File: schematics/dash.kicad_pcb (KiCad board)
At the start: 2 copper layers, 50 x 30 mm, 29 parts, among them J1 BATT_CONN, J2 EXTERNAL_TRIGGER, J3 USB_OTG, SW1 SW_Push, U1 ESP-12E, U2 ch340g, U3 MCP73833, U4 HT7333, Y1 12Mhz

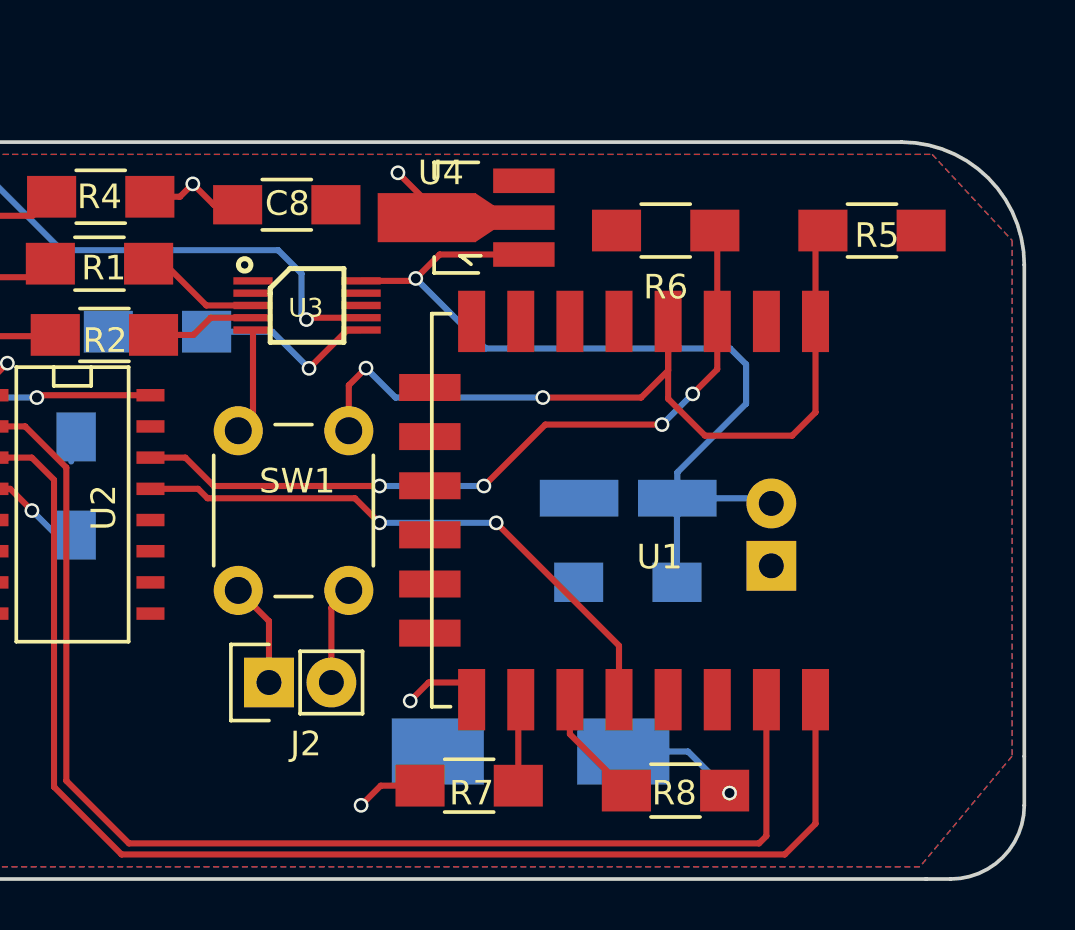
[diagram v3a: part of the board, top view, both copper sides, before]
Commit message: [fix] Correct wiring
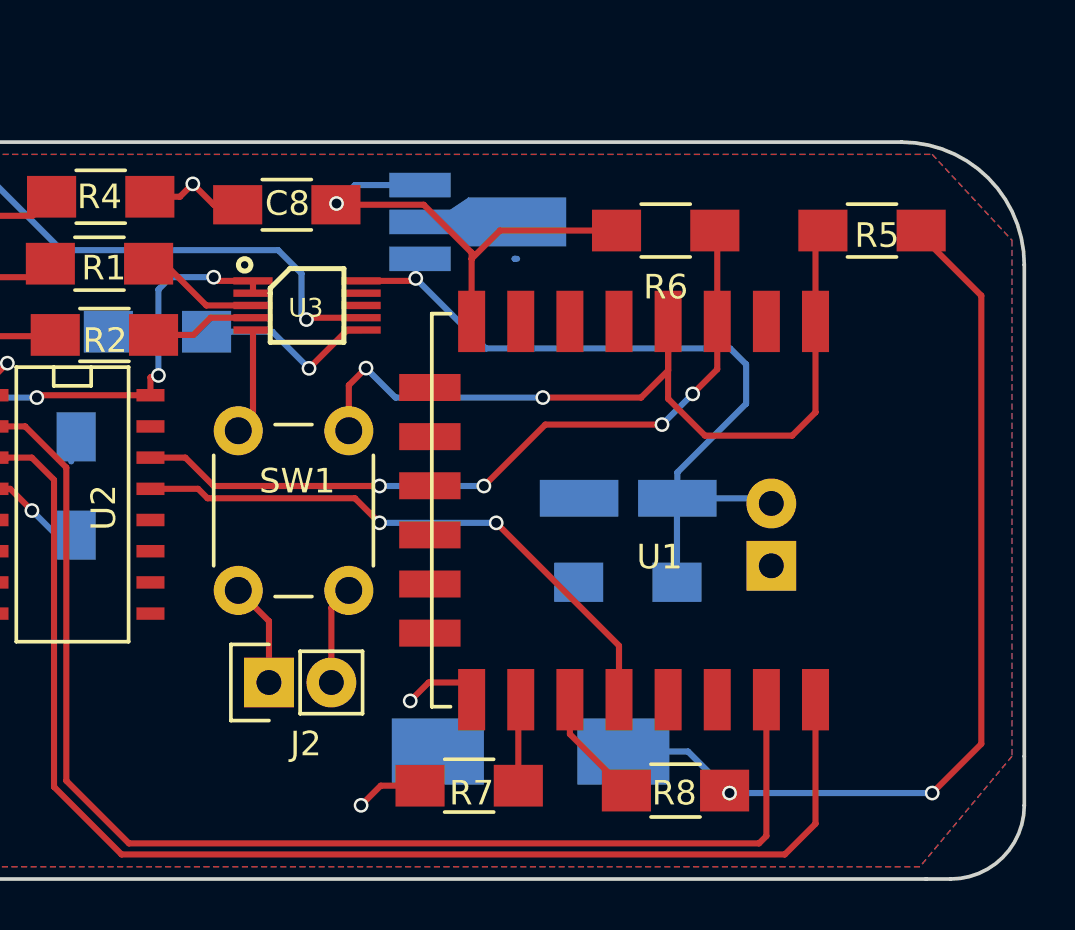
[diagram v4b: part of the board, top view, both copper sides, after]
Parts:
- U4: moved to B.Cu
- moved U4 0.51 mm to (152.8, 98.2)
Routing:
- net +3V3: track 5.27 -> 59.8 mm, vias 1 -> 3
- net +5V: track 26.9 -> 36.1 mm, vias 2 -> 4
- net Net-(C1-Pad1): track 35.9 -> 32.0 mm
- net GND: track 24.6 -> 22.3 mm, vias 6 -> 5
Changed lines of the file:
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@@
   (general
     (links 68)
-    (no_connects 12)
+    (no_connects 5)
     (area 124.924999 94.924999 175.075001 125.075001)
     (thickness 1.6)
     (drawings 10)
-    (tracks 196)
+    (tracks 223)
     (zones 0)
     (modules 29)
@@
     (add_net "Net-(U3-Pad9)")
   )
-  (module TO_SOT_Packages_SMD:SOT89-3_Housing_Handsoldering (layer F.Cu)
-    (at 152.275 98.075 90)
+  (module TO_SOT_Packages_SMD:SOT89-3_Housing_Handsoldering (layer B.Cu)
+    (at 152.75 98.25 90)
     (descr "SOT89-3, Housing, Handsoldering,")
     (tags "SOT89-3, Housing, Handsoldering,")
     (attr smd)
-    (fp_text reference U4 (at 1.825 -1.025 360) (layer F.SilkS)
-      (effects (font (size 1 1) (thickness 0.15)))
-    )
-    (fp_text value HT7333 (at -0.14986 5.30098 90) (layer F.Fab)
-      (effects (font (size 1 1) (thickness 0.15)))
-    )
-    (fp_line (start -1.89992 0.20066) (end -1.651 -0.09906) (layer F.SilkS) (width 0.15))
-    (fp_line (start -1.651 -0.09906) (end -1.5494 -0.24892) (layer F.SilkS) (width 0.15))
-    (fp_line (start -1.5494 -0.24892) (end -1.5494 0.59944) (layer F.SilkS) (width 0.15))
-    (fp_line (start -2.25044 -1.30048) (end -2.25044 0.50038) (layer F.SilkS) (width 0.15))
-    (fp_line (start -2.25044 -1.30048) (end -1.6002 -1.30048) (layer F.SilkS) (width 0.15))
-    (fp_line (start 2.25044 -1.30048) (end 2.25044 0.50038) (layer F.SilkS) (width 0.15))
-    (fp_line (start 2.25044 -1.30048) (end 1.6002 -1.30048) (layer F.SilkS) (width 0.15))
-    (pad 1 smd rect (at -1.50114 2.35204 90) (size 1.00076 2.5019) (layers F.Cu F.Paste F.Mask)
+    (fp_text reference U4 (at 1.825 1.025 180) (layer B.SilkS)
+      (effects (font (size 1 1) (thickness 0.15)) (justify mirror))
+    )
+    (fp_text value HT7333 (at -0.14986 -5.30098 90) (layer B.Fab)
+      (effects (font (size 1 1) (thickness 0.15)) (justify mirror))
+    )
+    (fp_line (start -1.89992 -0.20066) (end -1.651 0.09906) (layer B.SilkS) (width 0.15))
+    (fp_line (start -1.651 0.09906) (end -1.5494 0.24892) (layer B.SilkS) (width 0.15))
+    (fp_line (start -1.5494 0.24892) (end -1.5494 -0.59944) (layer B.SilkS) (width 0.15))
+    (fp_line (start -2.25044 1.30048) (end -2.25044 -0.50038) (layer B.SilkS) (width 0.15))
+    (fp_line (start -2.25044 1.30048) (end -1.6002 1.30048) (layer B.SilkS) (width 0.15))
+    (fp_line (start 2.25044 1.30048) (end 2.25044 -0.50038) (layer B.SilkS) (width 0.15))
+    (fp_line (start 2.25044 1.30048) (end 1.6002 1.30048) (layer B.SilkS) (width 0.15))
+    (pad 1 smd rect (at -1.50114 -2.35204 90) (size 1.00076 2.5019) (layers B.Cu B.Paste B.Mask)
       (net 1 "Net-(C1-Pad1)"))
-    (pad 2 smd rect (at 0 2.35204 90) (size 1.00076 2.5019) (layers F.Cu F.Paste F.Mask)
-      (net 2 GND))
-    (pad 3 smd rect (at 1.50114 2.35204 90) (size 1.00076 2.5019) (layers F.Cu F.Paste F.Mask)
+    (pad 2 smd rect (at 0 -2.35204 90) (size 1.00076 2.5019) (layers B.Cu B.Paste B.Mask)
+      (net 2 GND))
+    (pad 3 smd rect (at 1.50114 -2.35204 90) (size 1.00076 2.5019) (layers B.Cu B.Paste B.Mask)
       (net 36 +3V3))
-    (pad 2 smd rect (at 0 -1.6002 90) (size 1.99898 4.0005) (layers F.Cu F.Paste F.Mask)
-      (net 2 GND))
-    (pad 2 smd trapezoid (at 0 0.7493 270) (size 1.50114 0.7493) (rect_delta 0 0.50038 ) (layers F.Cu F.Paste F.Mask)
+    (pad 2 smd rect (at 0 1.6002 90) (size 1.99898 4.0005) (layers B.Cu B.Paste B.Mask)
+      (net 2 GND))
+    (pad 2 smd trapezoid (at 0 -0.7493 270) (size 1.50114 0.7493) (rect_delta 0 -0.50038 ) (layers B.Cu B.Paste B.Mask)
       (net 2 GND))
     (model TO_SOT_Packages_SMD.3dshapes/SOT89-3_Housing_Handsoldering.wrl
@@
   (segment (start 95.71 54.35) (end 91.71 50.35) (width 0.25) (layer F.Cu) (net 0))
   (segment (start 129.6 120.8) (end 130 120.8) (width 0.25) (layer F.Cu) (net 0))
+  (segment (start 150.225 100.55) (end 150.225 99.9241) (width 0.25) (layer B.Cu) (net 1) (status 800000))
+  (segment (start 150.225 99.9241) (end 150.39796 99.75114) (width 0.25) (layer B.Cu) (net 1) (status C00000))
   (segment (start 160.86 112.92) (end 160.86 109.515) (width 0.25) (layer B.Cu) (net 1))
   (segment (start 160.86 109.515) (end 160.875 109.5) (width 0.25) (layer B.Cu) (net 1))
-  (segment (start 154.62704 99.57614) (end 151.19886 99.57614) (width 0.25) (layer F.Cu) (net 1))
-  (segment (start 151.19886 99.57614) (end 150.225 100.55) (width 0.25) (layer F.Cu) (net 1))
   (segment (start 160.875 109.5) (end 160.875 108.45) (width 0.25) (layer B.Cu) (net 1))
   (segment (start 150.125 100.65) (end 148 100.65) (width 0.25) (layer F.Cu) (net 1))
@@
   (segment (start 142.975 97.55) (end 142 97.55) (width 0.25) (layer F.Cu) (net 2))
   (segment (start 142 97.55) (end 141.15 96.7) (width 0.25) (layer F.Cu) (net 2))
-  (segment (start 150.6748 98.075) (end 150.6748 97.4248) (width 0.25) (layer F.Cu) (net 2))
-  (segment (start 150.6748 97.4248) (end 149.5 96.25) (width 0.25) (layer F.Cu) (net 2))
-  (via (at 149.5 96.25) (size 0.6) (drill 0.4) (layers F.Cu B.Cu) (net 2))
   (segment (start 139.4 97.225) (end 140.625 97.225) (width 0.25) (layer F.Cu) (net 2))
   (via (at 141.15 96.7) (size 0.6) (drill 0.4) (layers F.Cu B.Cu) (net 2))
@@
   (segment (start 166.5 122.75) (end 165.25 124) (width 0.25) (layer F.Cu) (net 28))
   (segment (start 133.075 107.845) (end 133.595 107.845) (width 0.25) (layer F.Cu) (net 28))
+  (segment (start 143.6 100.65) (end 143.6 101.15) (width 0.25) (layer F.Cu) (net 35) (status C00000))
+  (segment (start 139.425 105.305) (end 139.425 104.575) (width 0.25) (layer F.Cu) (net 35) (status 400000))
+  (segment (start 142.15 100.65) (end 143.6 100.65) (width 0.25) (layer F.Cu) (net 35) (status 800000))
+  (segment (start 142 100.5) (end 142.15 100.65) (width 0.25) (layer F.Cu) (net 35))
+  (via (at 142 100.5) (size 0.6) (drill 0.4) (layers F.Cu B.Cu) (net 35))
+  (segment (start 140.25 100.5) (end 142 100.5) (width 0.25) (layer B.Cu) (net 35))
+  (segment (start 139.75 101) (end 140.25 100.5) (width 0.25) (layer B.Cu) (net 35))
+  (segment (start 139.75 104.5) (end 139.75 101) (width 0.25) (layer B.Cu) (net 35))
+  (via (at 139.75 104.5) (size 0.6) (drill 0.4) (layers F.Cu B.Cu) (net 35))
+  (segment (start 139.425 104.575) (end 139.75 104.5) (width 0.25) (layer F.Cu) (net 35))
   (segment (start 128.18014 102.9) (end 128.18014 100.5) (width 0.25) (layer F.Cu) (net 35))
   (segment (start 130.8 108.2) (end 130.8 105.51986) (width 0.25) (layer F.Cu) (net 35))
@@
   (via (at 130.8 108.2) (size 0.6) (drill 0.4) (layers F.Cu B.Cu) (net 35))
   (segment (start 130.7991 108.1991) (end 130.8 108.2) (width 0.25) (layer F.Cu) (net 35))
+  (segment (start 170.8 98.6) (end 170.8 98.8) (width 0.25) (layer F.Cu) (net 36) (status C00000))
+  (segment (start 170.8 98.8) (end 173.25 101.25) (width 0.25) (layer F.Cu) (net 36) (status 400000))
+  (segment (start 173.25 101.25) (end 173.25 119.5) (width 0.25) (layer F.Cu) (net 36))
+  (segment (start 173.25 119.5) (end 171.25 121.5) (width 0.25) (layer F.Cu) (net 36))
+  (via (at 171.25 121.5) (size 0.6) (drill 0.4) (layers F.Cu B.Cu) (net 36))
+  (segment (start 171.25 121.5) (end 163 121.5) (width 0.25) (layer B.Cu) (net 36))
+  (segment (start 152.5 99.75) (end 152.5 99.5) (width 0.25) (layer F.Cu) (net 36))
+  (segment (start 150.55 97.55) (end 146.975 97.55) (width 0.25) (layer F.Cu) (net 36) (status 800000))
+  (segment (start 152.5 99.5) (end 150.55 97.55) (width 0.25) (layer F.Cu) (net 36))
+  (segment (start 152.5 103) (end 152.5 99.75) (width 0.25) (layer F.Cu) (net 36) (status 400000))
+  (segment (start 153.65 98.6) (end 158.4 98.6) (width 0.25) (layer F.Cu) (net 36) (status 800000))
+  (segment (start 152.5 99.75) (end 153.65 98.6) (width 0.25) (layer F.Cu) (net 36))
+  (segment (start 150.39796 96.74886) (end 147.75114 96.74886) (width 0.25) (layer B.Cu) (net 36) (status 400000))
+  (segment (start 147 97.5) (end 146.975 97.525) (width 0.25) (layer F.Cu) (net 36) (status C00000))
+  (via (at 147 97.5) (size 0.6) (drill 0.4) (layers F.Cu B.Cu) (net 36) (status 800000))
+  (segment (start 147.75114 96.74886) (end 147 97.5) (width 0.25) (layer B.Cu) (net 36))
+  (segment (start 146.975 97.525) (end 146.975 97.55) (width 0.25) (layer F.Cu) (net 36) (status C00000))
+  (segment (start 152.5 103) (end 152.5 101.5) (width 0.25) (layer F.Cu) (net 36))
+  (segment (start 154.25 99.75) (end 154.25114 99.75114) (width 0.25) (layer B.Cu) (net 36) (status 30))
+  (segment (start 154.25114 99.75114) (end 154.35204 99.75114) (width 0.25) (layer B.Cu) (net 36) (status 30))
   (segment (start 158.675 119.81) (end 161.31 119.81) (width 0.25) (layer B.Cu) (net 36))
   (segment (start 163 121.5) (end 162.9 121.4) (width 0.25) (layer F.Cu) (net 36))

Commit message: [fix] Last fixes
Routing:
- net (no net): track 15.2 -> 0.50 mm
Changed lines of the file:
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@@
     (thickness 1.6)
     (drawings 10)
-    (tracks 223)
+    (tracks 220)
     (zones 0)
     (modules 29)
@@
   (gr_line (start 175 120) (end 175 100) (angle 90) (layer Edge.Cuts) (width 0.15))
   (gr_line (start 130 125) (end 171 125) (angle 90) (layer Edge.Cuts) (width 0.15))
-  (segment (start 95.71 57.4) (end 95.71 55.35) (width 0.25) (layer F.Cu) (net 0))
-  (segment (start 87.71 50.35) (end 87.71 57.4) (width 0.25) (layer F.Cu) (net 0))
-  (segment (start 95.71 54.35) (end 91.71 50.35) (width 0.25) (layer F.Cu) (net 0))
   (segment (start 129.6 120.8) (end 130 120.8) (width 0.25) (layer F.Cu) (net 0))
-  (segment (start 150.225 100.55) (end 150.225 99.9241) (width 0.25) (layer B.Cu) (net 1) (status 800000))
-  (segment (start 150.225 99.9241) (end 150.39796 99.75114) (width 0.25) (layer B.Cu) (net 1) (status C00000))
+  (segment (start 154.25 99.75) (end 154.25114 99.75114) (width 0.25) (layer B.Cu) (net 0) (status 30))
+  (segment (start 154.25114 99.75114) (end 154.35204 99.75114) (width 0.25) (layer B.Cu) (net 0) (status 30))
+  (segment (start 150.225 100.55) (end 150.225 99.9241) (width 0.25) (layer B.Cu) (net 1))
+  (segment (start 150.225 99.9241) (end 150.39796 99.75114) (width 0.25) (layer B.Cu) (net 1))
   (segment (start 160.86 112.92) (end 160.86 109.515) (width 0.25) (layer B.Cu) (net 1))
   (segment (start 160.86 109.515) (end 160.875 109.5) (width 0.25) (layer B.Cu) (net 1))
@@
   (segment (start 166.5 122.75) (end 165.25 124) (width 0.25) (layer F.Cu) (net 28))
   (segment (start 133.075 107.845) (end 133.595 107.845) (width 0.25) (layer F.Cu) (net 28))
-  (segment (start 143.6 100.65) (end 143.6 101.15) (width 0.25) (layer F.Cu) (net 35) (status C00000))
-  (segment (start 139.425 105.305) (end 139.425 104.575) (width 0.25) (layer F.Cu) (net 35) (status 400000))
-  (segment (start 142.15 100.65) (end 143.6 100.65) (width 0.25) (layer F.Cu) (net 35) (status 800000))
+  (segment (start 143.6 100.65) (end 143.6 101.15) (width 0.25) (layer F.Cu) (net 35))
+  (segment (start 139.425 105.305) (end 139.425 104.575) (width 0.25) (layer F.Cu) (net 35))
+  (segment (start 142.15 100.65) (end 143.6 100.65) (width 0.25) (layer F.Cu) (net 35))
   (segment (start 142 100.5) (end 142.15 100.65) (width 0.25) (layer F.Cu) (net 35))
   (via (at 142 100.5) (size 0.6) (drill 0.4) (layers F.Cu B.Cu) (net 35))
@@
   (via (at 130.8 108.2) (size 0.6) (drill 0.4) (layers F.Cu B.Cu) (net 35))
   (segment (start 130.7991 108.1991) (end 130.8 108.2) (width 0.25) (layer F.Cu) (net 35))
-  (segment (start 170.8 98.6) (end 170.8 98.8) (width 0.25) (layer F.Cu) (net 36) (status C00000))
-  (segment (start 170.8 98.8) (end 173.25 101.25) (width 0.25) (layer F.Cu) (net 36) (status 400000))
+  (segment (start 170.8 98.6) (end 170.8 98.8) (width 0.25) (layer F.Cu) (net 36))
+  (segment (start 170.8 98.8) (end 173.25 101.25) (width 0.25) (layer F.Cu) (net 36))
   (segment (start 173.25 101.25) (end 173.25 119.5) (width 0.25) (layer F.Cu) (net 36))
   (segment (start 173.25 119.5) (end 171.25 121.5) (width 0.25) (layer F.Cu) (net 36))
@@
   (segment (start 171.25 121.5) (end 163 121.5) (width 0.25) (layer B.Cu) (net 36))
   (segment (start 152.5 99.75) (end 152.5 99.5) (width 0.25) (layer F.Cu) (net 36))
-  (segment (start 150.55 97.55) (end 146.975 97.55) (width 0.25) (layer F.Cu) (net 36) (status 800000))
+  (segment (start 150.55 97.55) (end 146.975 97.55) (width 0.25) (layer F.Cu) (net 36))
   (segment (start 152.5 99.5) (end 150.55 97.55) (width 0.25) (layer F.Cu) (net 36))
-  (segment (start 152.5 103) (end 152.5 99.75) (width 0.25) (layer F.Cu) (net 36) (status 400000))
-  (segment (start 153.65 98.6) (end 158.4 98.6) (width 0.25) (layer F.Cu) (net 36) (status 800000))
+  (segment (start 152.5 103) (end 152.5 99.75) (width 0.25) (layer F.Cu) (net 36))
+  (segment (start 153.65 98.6) (end 158.4 98.6) (width 0.25) (layer F.Cu) (net 36))
   (segment (start 152.5 99.75) (end 153.65 98.6) (width 0.25) (layer F.Cu) (net 36))
-  (segment (start 150.39796 96.74886) (end 147.75114 96.74886) (width 0.25) (layer B.Cu) (net 36) (status 400000))
-  (segment (start 147 97.5) (end 146.975 97.525) (width 0.25) (layer F.Cu) (net 36) (status C00000))
-  (via (at 147 97.5) (size 0.6) (drill 0.4) (layers F.Cu B.Cu) (net 36) (status 800000))
+  (segment (start 150.39796 96.74886) (end 147.75114 96.74886) (width 0.25) (layer B.Cu) (net 36))
+  (segment (start 147 97.5) (end 146.975 97.525) (width 0.25) (layer F.Cu) (net 36))
+  (via (at 147 97.5) (size 0.6) (drill 0.4) (layers F.Cu B.Cu) (net 36))
   (segment (start 147.75114 96.74886) (end 147 97.5) (width 0.25) (layer B.Cu) (net 36))
-  (segment (start 146.975 97.525) (end 146.975 97.55) (width 0.25) (layer F.Cu) (net 36) (status C00000))
+  (segment (start 146.975 97.525) (end 146.975 97.55) (width 0.25) (layer F.Cu) (net 36))
   (segment (start 152.5 103) (end 152.5 101.5) (width 0.25) (layer F.Cu) (net 36))
-  (segment (start 154.25 99.75) (end 154.25114 99.75114) (width 0.25) (layer B.Cu) (net 36) (status 30))
-  (segment (start 154.25114 99.75114) (end 154.35204 99.75114) (width 0.25) (layer B.Cu) (net 36) (status 30))
   (segment (start 158.675 119.81) (end 161.31 119.81) (width 0.25) (layer B.Cu) (net 36))
   (segment (start 163 121.5) (end 162.9 121.4) (width 0.25) (layer F.Cu) (net 36))
